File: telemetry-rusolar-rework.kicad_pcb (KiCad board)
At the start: 4 copper layers, 109.1 x 91.2 mm, 165 parts, among them IC1 TLV62569DBVR, IC3 USBLC6-2P6, IC4 TPS22917DBVR, IC5 TPS22917DBVR, IC6 TPS22917DBVR, J1 USART Debug, J10 JP, J11 USB_B_Micro, J12 I2C, J13 GR2, J14 GR1, J16 47219-2001, J17 N_GR1, J18 SWD, J19 ESP GPIOs, J2 SPI, J3 MDT420E01001, J4 53048-0210, J5 Power Out, J6 UART, J7 SF72S006VBAR2500, J9 53048-0210, U1 TPS54302, U2 TJA1051TK-3, U3 STM32H725VETx, U4 ESP32-WROOM-32U, Y1 50MHz

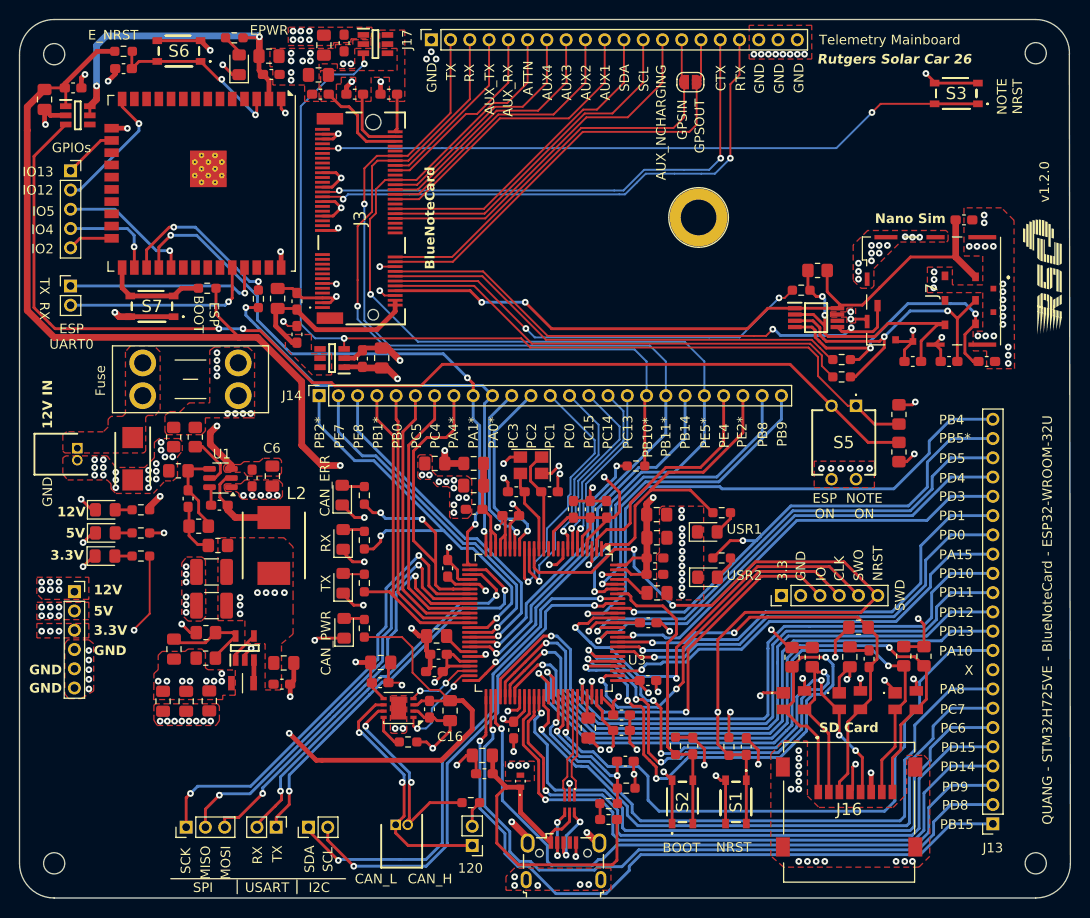
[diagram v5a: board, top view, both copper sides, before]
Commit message: Added AUX_EN, I2C com to Blues, LED labels
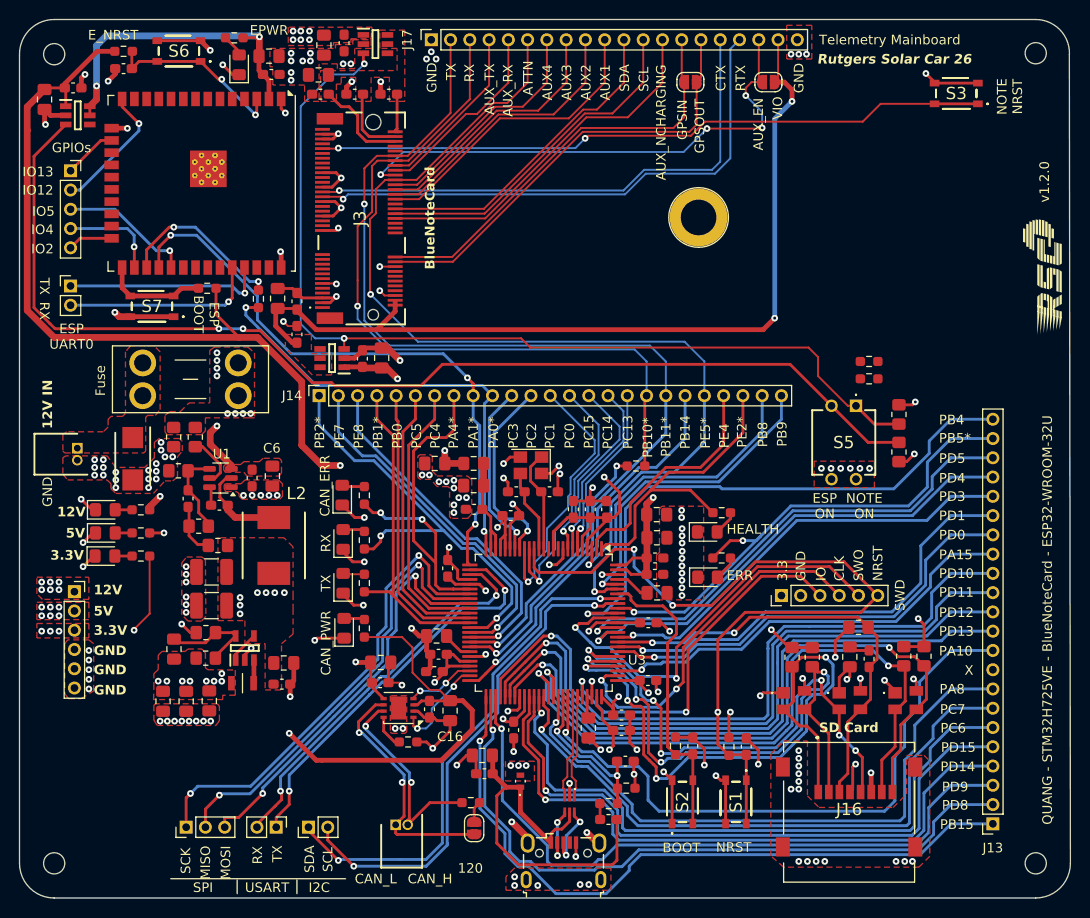
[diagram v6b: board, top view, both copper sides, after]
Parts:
- removed C22: 100n 16V, Capacitor_SMD:C_0603_1608Metric_Pad1.08x0.95mm_HandSolder
- removed C23, C24, C25: 33p 50V C0G, Capacitor_SMD:C_0603_1608Metric_Pad1.08x0.95mm_HandSolder
- removed D18: DT6250-06MR-13, SamacSys_Parts:SOP65P490X110-8N
- removed J10: JP, Connector_PinHeader_2.00mm:PinHeader_1x02_P2.00mm_Vertical
- removed J7: SF72S006VBAR2500, SamacSys_Parts:SF72S006VBAR2500
- removed R17: 15k, Resistor_SMD:R_0805_2012Metric_Pad1.20x1.40mm_HandSolder
- removed R18, R19, R25: 22, Resistor_SMD:R_0603_1608Metric_Pad0.98x0.95mm_HandSolder
- added JP2: SolderJumper_2_Open, Jumper:SolderJumper-2_P1.3mm_Open_RoundedPad1.0x1.5mm, F.Cu at (97.8, 95.4)
- added JP3: SolderJumper_2_Open, Jumper:SolderJumper-2_P1.3mm_Open_RoundedPad1.0x1.5mm, F.Cu at (67.2, 172.8)
- added R11: 100, Resistor_SMD:R_0603_1608Metric_Pad0.98x0.95mm_HandSolder, F.Cu at (108.2, 126.2)
- added R12: 100, Resistor_SMD:R_0603_1608Metric_Pad0.98x0.95mm_HandSolder, F.Cu at (108.2, 124.4)
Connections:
- net /PD12 renamed I2C4_SCL
- net /PD13 renamed I2C4_SDA
- J17 pad 18: GND -> /blue-note-card/AUX_EN
- J17 pad 19: GND -> +3.3V NOTE
- J3 pad 10: /blue-note-card/SIM_RST -> unconnected-(J3-Pad10)
- J3 pad 12: /blue-note-card/SIM_IO -> unconnected-(J3-Pad12)
- J3 pad 14: /blue-note-card/SIM_CLK -> unconnected-(J3-Pad14)
- J3 pad 16: /blue-note-card/SIM_NPRESENT -> unconnected-(J3-Pad16)
- J3 pad 40: /blue-note-card/SCL -> Net-(J3-Pad40)
- J3 pad 42: /blue-note-card/SDA -> Net-(J3-Pad42)
- J3 pad 56: unconnected-(J3-Pad56) -> /blue-note-card/AUX_EN
- J3 pad 8: /blue-note-card/SIM_VCC -> unconnected-(J3-Pad8)
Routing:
- net /blue-note-card/SIM_VCC: track 73.9 -> 0.00 mm, vias 2 -> 0
- net +3.3V NOTE: track 19.8 -> 92.7 mm, vias 0 -> 2
- net /blue-note-card/SIM_NPRESENT: track 58.9 -> 0.00 mm, vias 2 -> 0
- net /blue-note-card/AUX_EN: track 0.00 -> 54.5 mm, vias 0 -> 4
- net /blue-note-card/SIM_RST: track 50.0 -> 0.00 mm
- net /blue-note-card/SIM_CLK: track 49.0 -> 0.00 mm
- net /blue-note-card/SIM_IO: track 45.7 -> 0.00 mm, vias 2 -> 0
- net Net-(D18-I/O3): track 32.9 -> 0.00 mm, vias 2 -> 0
- net Net-(D18-I/O4): track 31.7 -> 0.00 mm, vias 2 -> 0
- net Net-(D18-I/O2): track 30.4 -> 0.00 mm, vias 2 -> 0
- net GND: track 216.3 -> 205.5 mm, vias 213 -> 171
- net Net-(JP3-A): track 2.77 -> 2.23 mm
- net /blue-note-card/CTX: track 55.1 -> 55.3 mm, vias 2 -> 1
- net /blue-note-card/RTX: track 57.0 -> 56.9 mm, vias 2 -> 1
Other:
- board text added: "AUX_EN"
- board text added: "ERR"
- board text added: "HEALTH"
- board text added: "PB5* -> ERR LED"
- board text added: "PE2* -> HEALTH LED"
- board text added: "VIO"
- board text removed: "Nano Sim"
- board text removed: "PB5* -> USR2 LED"
- board text removed: "PE2* -> USR1 LED"
- board text removed: "USR1"
- board text removed: "USR2"
